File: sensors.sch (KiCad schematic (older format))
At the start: 14 parts, among them U10 HMC5883L, U11 H3LIS331DL, U8 MS5611-01BA, U9 MPU6000

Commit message: schematic
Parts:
- C28, C29, C30, C31, C32, C33, C34, C35, C36: footprint (none) -> _std:_0603-W
- C37: footprint ~ -> _std:_0603-W
- U10: footprint MODULE -> _sensors:_HMC5883L
- U11: footprint MODULE -> _sensors:_H3LIS331DL
- U8: footprint MODULE -> _sensors:_MS5611-01BA
- U9: footprint MODULE -> _sensors:_MPU-60X0
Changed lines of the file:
@@
 F 0 "C30" H 2350 1950 50  0000 L CNN
 F 1 "0.1uF" H 2350 1750 50  0000 L CNN
-F 2 "" H 2300 1850 60  0001 C CNN
+F 2 "_std:_0603-W" H 2300 1850 60  0001 C CNN
 F 3 "" H 2300 1850 60  0001 C CNN
 	1    2300 1850
@@
 F 0 "U9" H 3600 4450 50  0000 C CNN
 F 1 "MPU6000" H 3600 4650 50  0000 C CNN
-F 2 "MODULE" H 3600 4550 50  0001 C CNN
+F 2 "_sensors:_MPU-60X0" H 3600 4550 50  0001 C CNN
 F 3 "DOCUMENTATION" H 3600 4550 50  0001 C CNN
 	1    3600 4550
@@
 F 0 "C28" H 1650 4450 50  0000 L CNN
 F 1 "0.1uF" H 1650 4250 50  0000 L CNN
-F 2 "" H 1600 4350 60  0001 C CNN
+F 2 "_std:_0603-W" H 1600 4350 60  0001 C CNN
 F 3 "" H 1600 4350 60  0001 C CNN
 	1    1600 4350
@@
 F 0 "C31" H 2500 4950 50  0000 L CNN
 F 1 "2.2nF 50V" V 2350 4650 50  0000 L CNN
-F 2 "" H 2450 4850 60  0001 C CNN
+F 2 "_std:_0603-W" H 2450 4850 60  0001 C CNN
 F 3 "" H 2450 4850 60  0001 C CNN
 	1    2450 4850
@@
 F 0 "C29" H 2150 4750 50  0000 L CNN
 F 1 "0.1uF" V 1950 4550 50  0000 L CNN
-F 2 "" H 2100 4650 60  0001 C CNN
+F 2 "_std:_0603-W" H 2100 4650 60  0001 C CNN
 F 3 "" H 2100 4650 60  0001 C CNN
 	1    2100 4650
@@
 F 0 "U10" H 8650 2150 50  0000 C CNN
 F 1 "HMC5883L" H 8000 2150 50  0000 C CNN
-F 2 "MODULE" H 8250 1800 50  0001 C CNN
+F 2 "_sensors:_HMC5883L" H 8250 1800 50  0001 C CNN
 F 3 "DOCUMENTATION" H 8250 1800 50  0001 C CNN
 	1    8250 1800
@@
 F 0 "C33" H 7300 2000 50  0000 L CNN
 F 1 "0.1uF" H 7300 1800 50  0000 L CNN
-F 2 "" H 7250 1900 60  0001 C CNN
+F 2 "_std:_0603-W" H 7250 1900 60  0001 C CNN
 F 3 "" H 7250 1900 60  0001 C CNN
 	1    7250 1900
@@
 F 0 "C32" H 7000 2000 50  0000 L CNN
 F 1 "0.1uF" H 7000 1800 50  0000 L CNN
-F 2 "" H 6950 1900 60  0001 C CNN
+F 2 "_std:_0603-W" H 6950 1900 60  0001 C CNN
 F 3 "" H 6950 1900 60  0001 C CNN
 	1    6950 1900
@@
 F 0 "C35" H 8200 2750 50  0000 L CNN
 F 1 "0.22uF" V 8050 2550 50  0000 L CNN
-F 2 "" H 8150 2650 60  0001 C CNN
+F 2 "_std:_0603-W" H 8150 2650 60  0001 C CNN
 F 3 "" H 8150 2650 60  0001 C CNN
 	1    8150 2650
@@
 F 0 "C36" H 8650 2600 50  0000 L CNN
 F 1 "4.7uF" V 8450 2400 50  0000 L CNN
-F 2 "" H 8600 2500 60  0001 C CNN
+F 2 "_std:_0603-W" H 8600 2500 60  0001 C CNN
 F 3 "" H 8600 2500 60  0001 C CNN
 	1    8600 2500
@@
 F 0 "U8" H 3500 2250 50  0000 C CNN
 F 1 "MS5611-01BA" H 3000 2250 50  0000 C CNN
-F 2 "MODULE" H 3150 1850 50  0001 C CNN
+F 2 "_sensors:_MS5611-01BA" H 3150 1850 50  0001 C CNN
 F 3 "DOCUMENTATION" H 3150 1850 50  0001 C CNN
 	1    3150 1850
@@
 F 0 "C34" H 7300 4650 50  0000 L CNN
 F 1 "0.1uF" H 7300 4450 50  0000 L CNN
-F 2 "" H 7250 4550 60  0001 C CNN
+F 2 "_std:_0603-W" H 7250 4550 60  0001 C CNN
 F 3 "" H 7250 4550 60  0001 C CNN
 	1    7250 4550
@@
 F 0 "U11" H 8800 5100 50  0000 C CNN
 F 1 "H3LIS331DL" H 8150 5100 50  0000 C CNN
-F 2 "MODULE" H 8550 4600 50  0001 C CNN
+F 2 "_sensors:_H3LIS331DL" H 8550 4600 50  0001 C CNN
 F 3 "high-g accelerometer" H 8550 4600 50  0001 C CNN
 	1    8400 4600
@@
 F 0 "C37" H 7000 4650 40  0000 L CNN
 F 1 "10uF" H 7006 4465 40  0000 L CNN
-F 2 "~" H 7038 4400 30  0000 C CNN
+F 2 "_std:_0603-W" H 7038 4400 30  0000 C CNN
 F 3 "~" H 7000 4550 60  0000 C CNN
 	1    7000 4550

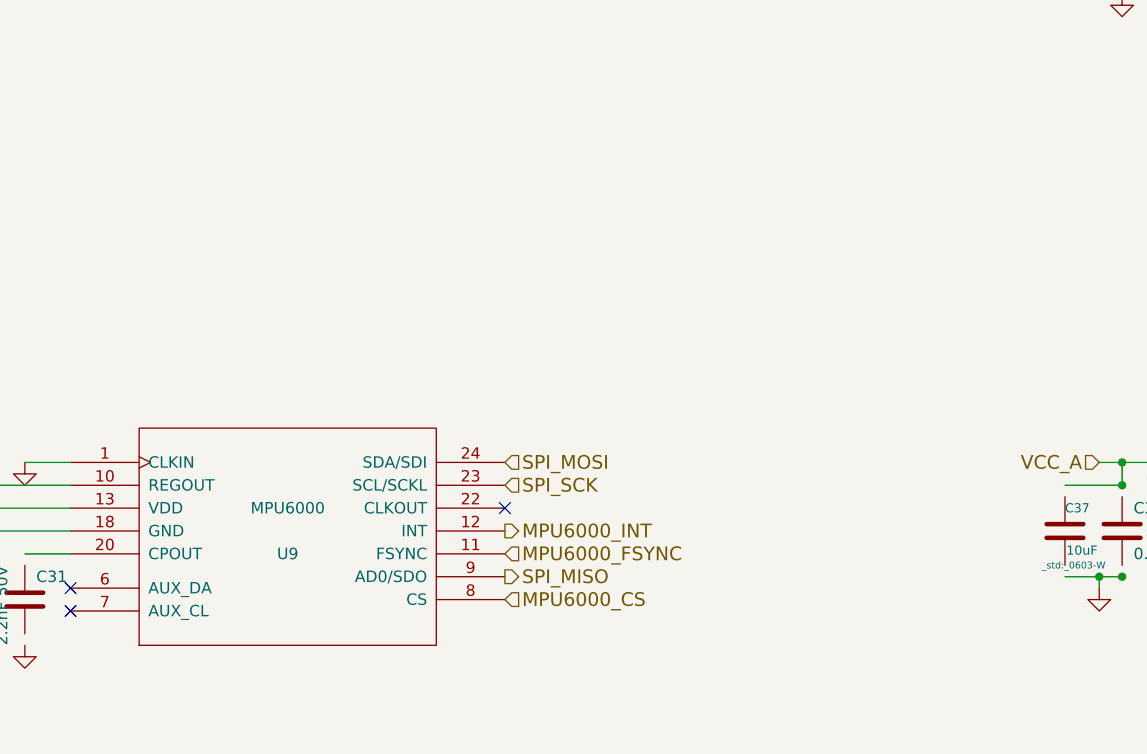
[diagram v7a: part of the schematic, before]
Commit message: comments power supply changes
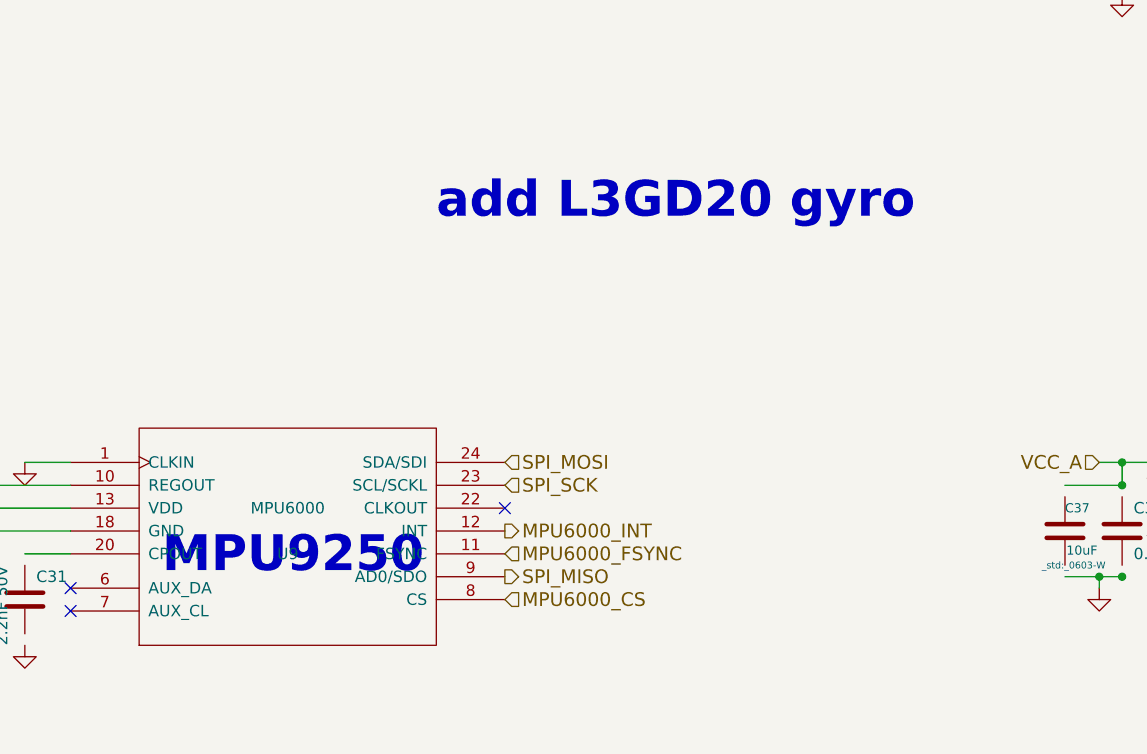
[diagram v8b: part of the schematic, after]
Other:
- note added: "MPU9250\n"
- note added: "add L3GD20 gyro\n"
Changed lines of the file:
@@
 LIBS:memory
 LIBS:xilinx
-LIBS:special
 LIBS:microcontrollers
 LIBS:dsp
@@
 Text HLabel 9100 4800 2    60   Input ~ 0
 VCC_A
+Text Notes 4250 3200 0    157  ~ 31
+add L3GD20 gyro\n
+Text Notes 3050 4750 0    157  ~ 31
+MPU9250\n
 $EndSCHEMATC
